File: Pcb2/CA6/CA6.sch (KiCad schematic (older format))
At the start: 119 parts, among them J1 MICRO_USB, J2 BAT_CON, J3 MODULE_0, J4 MODULE_2, J5 MODULE_1, J6 AUX, J7 AUX, J8 MODULE_3, P1 JTAG, P2 RFD22301 Breakout, Q1 BSS138P, Q10 BSS138P, Q11 BSS138P, Q12 BSS138P, Q13 BSS138P, Q14 BSS138P, Q15 BSS138P, Q16 BSS138P, Q2 BSS138P, Q3 BSS138P, Q4 BSS138P, Q5 BSS138P, Q6 BSS138P, Q7 BSS138P, Q8 BSS138P, Q9 BSS138P, SW1 ERASE, SW2 USB/BATTERY, SW3 RESET, U12 VREG_33, U14 EEPROM, U15 L_PIPE, U16 ATSAM3X8EA-AU_LQFP-144, U17 RFD22301, X1 HOLE, X10 DP, X2 HOLE, X3 HOLE, X4 DP, X6 DP, X7 CRYSTAL_4, X8 32khz, X9 DP

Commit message: Clear out old traces and make it a 2 layer board
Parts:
- removed X10, X4, X6, X9: DP, CA6:DUMMY_PIN_NEPAD_1MM, symbol DUMMY_PIN
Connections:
- no-connect marks 9 -> 14
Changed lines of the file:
@@
 AUX43
-$Comp
-L DUMMY_PIN X4
-U 1 1 5424AE5A
-P 13500 8350
-F 0 "X4" H 13950 8350 60  0000 C CNN
-F 1 "DP" H 13750 8350 60  0001 C CNN
-F 2 "CA6:DUMMY_PIN_NEPAD_1MM" H 13500 8350 60  0001 C CNN
-F 3 "~" H 13500 8350 60  0000 C CNN
-	1    13500 8350
-	1    0    0    -1
-$EndComp
-$Comp
-L DUMMY_PIN X10
-U 1 1 5424AF6F
-P 13500 8450
-F 0 "X10" H 13950 8450 60  0000 C CNN
-F 1 "DP" H 13750 8450 60  0001 C CNN
-F 2 "CA6:DUMMY_PIN_NEPAD_1MM" H 13500 8450 60  0001 C CNN
-F 3 "~" H 13500 8450 60  0000 C CNN
-	1    13500 8450
-	1    0    0    -1
-$EndComp
-$Comp
-L DUMMY_PIN X6
-U 1 1 5424AF75
-P 8400 9250
-F 0 "X6" H 8850 9250 60  0000 C CNN
-F 1 "DP" H 8650 9250 60  0001 C CNN
-F 2 "CA6:DUMMY_PIN_NEPAD_1MM" H 8400 9250 60  0001 C CNN
-F 3 "~" H 8400 9250 60  0000 C CNN
-	1    8400 9250
-	-1   0    0    1
-$EndComp
-$Comp
-L DUMMY_PIN X9
-U 1 1 5424AF81
-P 13500 6550
-F 0 "X9" H 13950 6550 60  0000 C CNN
-F 1 "DP" H 13750 6550 60  0001 C CNN
-F 2 "CA6:DUMMY_PIN_NEPAD_1MM" H 13500 6550 60  0001 C CNN
-F 3 "~" H 13500 6550 60  0000 C CNN
-	1    13500 6550
-	1    0    0    -1
-$EndComp
 $Comp
 L R R30
@@
 Connection ~ 2250 13300
 Connection ~ 1950 13600
+NoConn ~ 13500 6550
+NoConn ~ 13500 8350
+NoConn ~ 13500 8450
+NoConn ~ 8400 9250
+NoConn ~ 21400 4200
 $EndSCHEMATC

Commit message: Remove link port, only support 3.3V on aux, make board bigger, make board 2 layers, add camera port leds
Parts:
- removed C16, C35: 10uf, CA6:c_1206, symbol C
- removed D3: SCH_D, CA6:SM1206-D-A, symbol DIODESCH
- removed LP1: LINK_RJ10, CA6:RJ10_A-2004-3-4-LP-N-R, symbol JACK_RJ10
- removed R23, R24: 10k, CA6:SM0603_Resistor, symbol R
- added D10, D2, D4, D5, D6, D7, D8, D9: LED, LEDs:LED_0805, symbol LED
- added R1, R2, R3, R4, R5, R6, R7, R8: 680R, CA6:SM0603_Resistor, symbol R
- added U1, U2, U3, U4, U5, U6, U7, U8: L_PIPE, CA6:SLP3-150-100-R, symbol LED_LIGHT_PIPE
- added X4: HOLE, CA6:HOLE_3.0mm, symbol HOLE
- LOGO2: footprint CA6:CA_Logo_Mirror_15mm -> CA6:CA_Logo_15mm
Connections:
- net 3V3: now also J6.48 (PIN48), J7.48 (PIN48)
- net 5V: no longer J6.48 (PIN48), J7.48 (PIN48)
- net CAM0S: now also R1.1
- net CAM1S: now also R2.1
- net CAM2S: now also R3.1
- net CAM3S: now also R4.1
- net CAM4S: now also R5.1
- net CAM5S: now also R6.1
- net CAM6S: now also R7.1
- net CAM7S: now also R8.1
- net GND: now also D10.1 (K), D2.1 (K), D4.1 (K), D5.1 (K), D6.1 (K), D7.1 (K), D8.1 (K), D9.1 (K)
- new net: D2.2 (A), R1.2
- new net: D4.2 (A), R2.2
- new net: D5.2 (A), R3.2
- new net: D6.2 (A), R4.2
- new net: D7.2 (A), R5.2
- new net: D8.2 (A), R6.2
- new net: D9.2 (A), R7.2
- new net: D10.2 (A), R8.2
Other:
- note removed: "Link Port"

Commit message: Lots more small changes to the pcb
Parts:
- removed BT1: 4xAA_BATTERY_HOLDER, CA6:BATTERY_4AA_12BH348-GR, symbol BATTERY
- removed C26: 10uf, CA6:c_1206, symbol C
- removed C27: 0.1uf, CA6:c_0603, symbol C
- removed FTDI_2: FTDI_BLE, CA6:SIL-6, symbol FTDI
- removed U17: RFD22301, CA6:RFD22301, symbol RFD22301
- P2: footprint CA6:JTAG_20021121-00010C4LF -> Socket_Strips:Socket_Strip_Straight_2x05_Pitch2.54mm
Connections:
- net 3V3: now also C23.1, C34.1, P2.2 (PIN2); no longer C23.2, C34.2, P2.8 (PIN8)
- net GND: now also C23.2, C34.2, P2.1 (PIN1); no longer C23.1, C34.1, P2.10 (PIN10), P2.9 (PIN9)
- net at U16.13 (PD0): no longer R22.1
- net at U16.14 (PD1): no longer R30.1
- net BLE_CTS: no longer names the net of P2.4 (PIN4)
- net BLE_CTS: now also R30.1; no longer U16.8 (PA15)
- net BLE_GPIO4 renamed CC_TX
- net CC_TX: now also U16.6 (PA13)
- net BLE_GPIO5: no longer names the net of P2.6 (PIN6)
- net BLE_GPIO5: now also R22.1
- net BLE_GPIO6 renamed CC_RTS
- net CC_RTS: now also U16.7 (PA14)
- net BLE_RTS renamed CC_RX
- net CC_RX: now also U16.5 (PA12); no longer U16.7 (PA14)
- removed net BLE_RX: P2.2 (PIN2), U16.5 (PA12)
- removed net BLE_TX: P2.1 (PIN1), U16.6 (PA13)
- net LP_FOCUS: no longer names the net of U16.59 (PC2)
- net LP_SHUTTER: no longer names the net of U16.60 (PC3)
- new net CC_CTS: P2.9 (PIN9), U16.8 (PA15)
- new net CC_PROG: P2.10 (PIN10)
- new net CC_RESET: P2.8 (PIN8)
- no-connect marks 14 -> 8
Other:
- note added: "Connectivity Card"
- note removed: "Bluetooth"
- moved on the sheet: C23, C30, C31, C32, C33, C34, C37, D1, J3, J4, J5, J6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

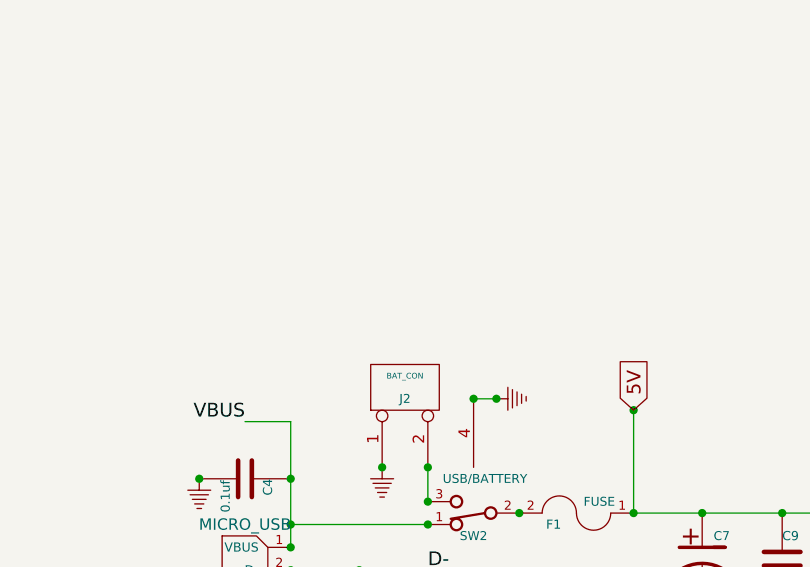
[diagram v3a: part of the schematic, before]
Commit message: Clean up layout and add ground plane
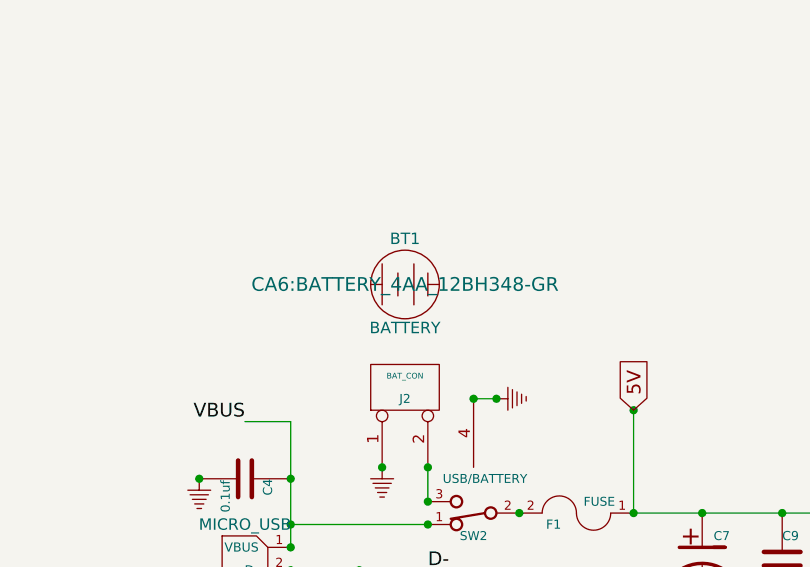
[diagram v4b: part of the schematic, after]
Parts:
- added BT1: BATTERY, CA6:BATTERY_4AA_12BH348-GR, symbol BATTERY
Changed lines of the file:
@@
 	18200 12700 18150 12700
 Connection ~ 18150 12700
+$Comp
+L BATTERY BT1
+U 1 1 58D3FF70
+P 7400 12800
+F 0 "BT1" H 7400 13000 50  0000 C CNN
+F 1 "BATTERY" H 7400 12610 50  0000 C CNN
+F 2 "CA6:BATTERY_4AA_12BH348-GR" H 7400 12800 60  0000 C CNN
+F 3 "" H 7400 12800 60  0000 C CNN
+	1    7400 12800
+	1    0    0    -1
+$EndComp
 $EndSCHEMATC

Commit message: Routing pcb
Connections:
- net 3V3: no longer J6.48 (PIN48), J7.48 (PIN48)
- net AUX02: now also U16.141 (PB22); no longer U16.136 (PC25)
- net AUX03: now also U16.140 (PB14); no longer U16.135 (PC24)
- net AUX04: now also U16.138 (PC27); no longer U16.134 (PC23)
- net AUX05: now also U16.137 (PC26); no longer U16.133 (PC22)
- net AUX06: now also U16.136 (PC25); no longer U16.132 (PC21)
- net AUX07: now also U16.135 (PC24); no longer U16.131 (PC20)
- net AUX08: now also U16.134 (PC23); no longer U16.128 (PB10)
- net AUX09: now also U16.133 (PC22); no longer U16.127 (PB9)
- net AUX10: now also U16.132 (PC21); no longer U16.123 (PB8)
- net AUX11: now also U16.131 (PC20); no longer U16.122 (PB7)
- net AUX12: now also U16.128 (PB10); no longer U16.121 (PB6)
- net AUX13: now also U16.127 (PB9); no longer U16.120 (PB5)
- net AUX14: now also U16.123 (PB8); no longer U16.119 (PB4)
- net AUX15: now also U16.122 (PB7); no longer U16.118 (PB3)
- net AUX16: now also U16.121 (PB6); no longer U16.117 (PC10)
- net AUX17: now also U16.120 (PB5); no longer U16.116 (PC4)
- net AUX18: now also U16.119 (PB4); no longer U16.115 (PB2)
- net AUX19: now also U16.118 (PB3); no longer U16.114 (PB1)
- net AUX20: now also U16.117 (PC10); no longer U16.113 (PB0)
- net AUX21: now also U16.116 (PC4); no longer U16.112 (PA29)
- net AUX22: now also U16.115 (PB2); no longer U16.103 (PC30)
- net AUX23: now also U16.114 (PB1); no longer U16.102 (PC29)
- net AUX24: now also U16.113 (PB0); no longer U16.101 (PC19)
- net AUX25: now also U16.112 (PA29); no longer U16.100 (PC18)
- net AUX26: now also U16.103 (PC30); no longer U16.99 (PC17)
- net AUX27: now also U16.102 (PC29); no longer U16.98 (PC16)
- net AUX28: now also U16.101 (PC19); no longer U16.97 (PC15)
- net AUX29: now also U16.100 (PC18); no longer U16.96 (PC14)
- net AUX30: now also U16.99 (PC17); no longer U16.95 (PC13)
- net AUX31: now also U16.98 (PC16); no longer U16.94 (PC12)
- net AUX32: now also U16.97 (PC15); no longer U16.93 (PC11)
- net AUX33: now also U16.96 (PC14); no longer U16.92 (PB21)
- net AUX34: now also U16.95 (PC13); no longer U16.91 (PB20)
- net AUX35: now also U16.94 (PC12); no longer U16.90 (PB19)
- net AUX36: now also U16.93 (PC11); no longer U16.89 (PB18)
- net AUX37: now also U16.92 (PB21); no longer U16.77 (PB16)
- net AUX38: now also U16.91 (PB20); no longer U16.76 (PB15)
- net AUX39: now also U16.90 (PB19); no longer U16.72 (PA20)
- net AUX40: now also U16.89 (PB18); no longer U16.71 (PA19)
- net AUX41: now also U16.77 (PB16); no longer U16.68 (PB27)
- net AUX42: now also U16.76 (PB15); no longer U16.67 (PC9)
- net AUX43: now also U16.72 (PA20); no longer U16.66 (PC8)
- net AUX_RX: now also J6.2 (PIN2), J7.2 (PIN2); no longer J6.46 (PIN46), J7.46 (PIN46)
- net AUX_TX: now also J6.1 (PIN1), J7.1 (PIN1); no longer J6.45 (PIN45), J7.45 (PIN45)
- net CAM0F: now also U16.142 (PB23); no longer U16.140 (PB14)
- net CAM0S: now also U16.143 (PB24); no longer U16.141 (PB22)
- net CAM1F: now also U16.144 (PB25); no longer U16.142 (PB23)
- net CAM1S: now also U16.1 (PB26); no longer U16.143 (PB24)
- net CAM2F: now also U16.13 (PD0); no longer U16.144 (PB25)
- net CAM2S: now also U16.14 (PD1); no longer U16.1 (PB26)
- net CC_PROG: now also U16.59 (PC2)
- net CC_RESET: now also U16.55 (PC1)
- net GND: no longer J6.47 (PIN47), J7.47 (PIN47)
- net MOD3_ID: now also U16.60 (PC3); no longer U16.55 (PC1)
- removed net AUX00: J6.1 (PIN1), J7.1 (PIN1), U16.138 (PC27)
- removed net AUX01: J6.2 (PIN2), J7.2 (PIN2), U16.137 (PC26)
- new net AUX44: J6.45 (PIN45), J7.45 (PIN45), U16.71 (PA19)
- new net AUX45: J6.46 (PIN46), J7.46 (PIN46), U16.68 (PB27)
- new net AUX46: J6.47 (PIN47), J7.47 (PIN47), U16.67 (PC9)
- new net AUX47: J6.48 (PIN48), J7.48 (PIN48), U16.66 (PC8)
- no-connect marks 8 -> 7
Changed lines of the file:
@@
 Text Notes 1900 3350 0    118  ~ 24
 JTAG
-Text Notes 18500 14200 0    118  ~ 24
+Text Notes 18850 13900 0    118  ~ 24
 Connectivity Card
 Text Notes 9000 15350 0    118  ~ 24
@@
 	0    -1   -1   0
 $EndComp
-Text Label 13650 900  0    60   ~ 0
-AUX01
+Text Label 13650 3100 0    60   ~ 0
+AUX45
 Text Label 3650 2350 0    60   ~ 0
 JTAG_TMS
@@
 Text Label 6900 2550 2    60   ~ 0
 EEPROM_ID
-Text Label 12150 900  2    60   ~ 0
-AUX00
+Text Label 12150 3100 2    60   ~ 0
+AUX44
 Text Label 12150 1000 2    60   ~ 0
 AUX02
@@
 Text Label 13650 1800 0    60   ~ 0
 AUX19
-Text Label 8400 9150 2    60   ~ 0
-AUX00
 Text Label 19250 6300 0    60   ~ 0
 MOD0_AN1
@@
 Text Label 9200 5750 1    60   ~ 0
 MOD3_MISO
-Text Label 8400 7350 2    60   ~ 0
+Text Label 8400 8050 2    60   ~ 0
 AUX13
-Text Label 8400 7250 2    60   ~ 0
+Text Label 8400 7650 2    60   ~ 0
 AUX14
-Text Label 8400 7150 2    60   ~ 0
+Text Label 8400 7550 2    60   ~ 0
 AUX15
-Text Label 8400 7050 2    60   ~ 0
+Text Label 8400 7450 2    60   ~ 0
 AUX16
-Text Label 8400 6950 2    60   ~ 0
+Text Label 8400 7350 2    60   ~ 0
 AUX17
-Text Label 8400 6850 2    60   ~ 0
+Text Label 8400 7250 2    60   ~ 0
 AUX18
-Text Label 8400 6750 2    60   ~ 0
+Text Label 8400 7150 2    60   ~ 0
 AUX19
-Text Label 8400 6650 2    60   ~ 0
+Text Label 8400 7050 2    60   ~ 0
 AUX20
-Text Label 8400 6550 2    60   ~ 0
+Text Label 8400 6950 2    60   ~ 0
 AUX21
-Text Label 9700 5750 1    60   ~ 0
+Text Label 8400 6850 2    60   ~ 0
 AUX22
-Text Label 9800 5750 1    60   ~ 0
+Text Label 8400 6750 2    60   ~ 0
 AUX23
-Text Label 9900 5750 1    60   ~ 0
+Text Label 8400 6650 2    60   ~ 0
 AUX24
-Text Label 10000 5750 1    60   ~ 0
+Text Label 8400 6550 2    60   ~ 0
 AUX25
-Text Label 10100 5750 1    60   ~ 0
+Text Label 9700 5750 1    60   ~ 0
 AUX26
-Text Label 10200 5750 1    60   ~ 0
+Text Label 9800 5750 1    60   ~ 0
 AUX27
 Text Label 11300 5750 1    60   ~ 0
@@
 Text Label 9300 5750 1    60   ~ 0
 EEPROM_ID
-Text Label 8400 9350 2    60   ~ 0
+Text Label 8400 9550 2    60   ~ 0
 CAM0F
-Text Label 8400 9450 2    60   ~ 0
+Text Label 8400 9650 2    60   ~ 0
 CAM0S
-Text Label 8400 9550 2    60   ~ 0
+Text Label 8400 9750 2    60   ~ 0
 CAM1F
-Text Label 8400 9650 2    60   ~ 0
+Text Label 9200 10250 3    60   ~ 0
 CAM1S
 Text Label 8400 8250 2    60   ~ 0
 UOTGID
-Text Label 8400 9750 2    60   ~ 0
+Text Label 10400 10250 3    60   ~ 0
 CAM2F
-Text Label 9200 10250 3    60   ~ 0
+Text Label 10500 10250 3    60   ~ 0
 CAM2S
 Text Label 10600 10250 3    60   ~ 0
@@
 Text Label 12200 5750 1    60   ~ 0
 MOD3_AN1
-Text Label 10300 5750 1    60   ~ 0
+Text Label 9900 5750 1    60   ~ 0
 AUX28
-Text Label 10400 5750 1    60   ~ 0
+Text Label 10000 5750 1    60   ~ 0
 AUX29
-Text Label 10800 5750 1    60   ~ 0
+Text Label 10400 5750 1    60   ~ 0
 AUX33
-Text Label 10900 5750 1    60   ~ 0
+Text Label 10500 5750 1    60   ~ 0
 AUX34
 $Comp
@@
 	1    0    0    -1
 $EndComp
-Text Label 11100 5750 1    60   ~ 0
+Text Label 10700 5750 1    60   ~ 0
 AUX36
-Text Label 12400 5750 1    60   ~ 0
+Text Label 10900 5750 1    60   ~ 0
 AUX38
 Text Label 11800 10250 3    60   ~ 0
 AUX_RX
-Text Label 11000 5750 1    60   ~ 0
+Text Label 10600 5750 1    60   ~ 0
 AUX35
 $Comp
@@
 	1    0    0    -1
 $EndComp
-Text Label 12150 3100 2    60   ~ 0
+Text Label 12150 900  2    60   ~ 0
 AUX_TX
 $Comp
@@
 Text Label 21100 7750 2    60   ~ 0
 MOD3_CS
-Text Label 12300 5750 1    60   ~ 0
+Text Label 10800 5750 1    60   ~ 0
 AUX37
-Text Label 8400 9050 2    60   ~ 0
-AUX01
-Text Label 8400 8950 2    60   ~ 0
+Text Label 8400 9450 2    60   ~ 0
 AUX02
-Text Label 8400 8850 2    60   ~ 0
+Text Label 8400 9350 2    60   ~ 0
 AUX03
-Text Label 8400 8750 2    60   ~ 0
+Text Label 8400 9150 2    60   ~ 0
 AUX04
-Text Label 8400 8650 2    60   ~ 0
+Text Label 8400 9050 2    60   ~ 0
 AUX05
-Text Label 8400 8550 2    60   ~ 0
+Text Label 8400 8950 2    60   ~ 0
 AUX06
-Text Label 8400 8450 2    60   ~ 0
+Text Label 8400 8850 2    60   ~ 0
 AUX07
-Text Label 8400 8150 2    60   ~ 0
+Text Label 8400 8750 2    60   ~ 0
 AUX08
-Text Label 8400 8050 2    60   ~ 0
+Text Label 8400 8650 2    60   ~ 0
 AUX09
-Text Label 8400 7650 2    60   ~ 0
+Text Label 8400 8550 2    60   ~ 0
 AUX10
-Text Label 8400 7450 2    60   ~ 0
+Text Label 8400 8150 2    60   ~ 0
 AUX12
-Text Label 8400 7550 2    60   ~ 0
+Text Label 8400 8450 2    60   ~ 0
 AUX11
 Text Label 13500 7150 0    60   ~ 0
 MOD2_ID
-Text Label 10700 5750 1    60   ~ 0
+Text Label 10300 5750 1    60   ~ 0
 AUX32
-Text Label 10600 5750 1    60   ~ 0
+Text Label 10200 5750 1    60   ~ 0
 AUX31
-Text Label 10500 5750 1    60   ~ 0
+Text Label 10100 5750 1    60   ~ 0
 AUX30
 $Comp
@@
 	1    0    0    -1
 $EndComp
-Text Label 13500 7950 0    60   ~ 0
+Text Label 13500 7450 0    60   ~ 0
 MOD3_ID
 $Comp
@@
 	1    0    0    -1
 $EndComp
-Text Label 13650 3100 0    60   ~ 0
+Text Label 13650 900  0    60   ~ 0
 AUX_RX
-Text Label 16450 900  0    60   ~ 0
-AUX01
-Text Label 14950 900  2    60   ~ 0
-AUX00
 Text Label 14950 1000 2    60   ~ 0
 AUX02
@@
 Text Label 16450 3000 0    60   ~ 0
 AUX43
-Text Label 14950 3100 2    60   ~ 0
+Text Label 14950 900  2    60   ~ 0
 AUX_TX
 $Comp
@@
 	1    0    0    -1
 $EndComp
-Text Label 16450 3100 0    60   ~ 0
+Text Label 16450 900  0    60   ~ 0
 AUX_RX
 $Comp
@@
 	1    0    0    -1
 $EndComp
-Text Label 13500 6650 0    60   ~ 0
+Text Label 12300 5750 1    60   ~ 0
 AUX41
-Text Label 13500 6250 0    60   ~ 0
+Text Label 11000 5750 1    60   ~ 0
 AUX39
-Text Label 13500 6350 0    60   ~ 0
+Text Label 11100 5750 1    60   ~ 0
 AUX40
-Text Label 13500 6750 0    60   ~ 0
+Text Label 12400 5750 1    60   ~ 0
 AUX42
-Text Label 13500 6850 0    60   ~ 0
+Text Label 13500 6250 0    60   ~ 0
 AUX43
 $Comp
@@
 Connection ~ 13650 3700
 Connection ~ 12150 3300
-Connection ~ 12150 900
-Connection ~ 12150 1000
-Connection ~ 12150 1100
-Connection ~ 12150 1200
-Connection ~ 12150 1300
-Connection ~ 12150 1400
-Connection ~ 12150 1500
-Connection ~ 12150 1600
-Connection ~ 12150 1700
-Connection ~ 12150 1800
-Connection ~ 12150 1900
-Connection ~ 12150 2000
-Connection ~ 12150 2100
-Connection ~ 12150 2200
-Connection ~ 12150 2300
-Connection ~ 12150 2400
-Connection ~ 12150 2500
-Connection ~ 12150 2600
-Connection ~ 12150 2700
-Connection ~ 12150 2800
-Connection ~ 12150 2900
-Connection ~ 12150 3000
-Connection ~ 12150 3100
-Connection ~ 12150 3200
-Connection ~ 13650 3000
-Connection ~ 13650 2900
-Connection ~ 13650 2800
-Connection ~ 13650 2700
-Connection ~ 13650 2600
-Connection ~ 13650 2500
-Connection ~ 13650 2400
-Connection ~ 13650 2300
-Connection ~ 13650 2200
-Connection ~ 13650 2100
-Connection ~ 13650 2000
-Connection ~ 13650 1900
-Connection ~ 13650 1800
-Connection ~ 13650 1700
-Connection ~ 13650 1600
-Connection ~ 13650 1500
-Connection ~ 13650 1400
-Connection ~ 13650 1300
-Connection ~ 13650 1200
-Connection ~ 13650 1100
-Connection ~ 13650 1000
-Connection ~ 13650 900
 Connection ~ 8400 13350
 Connection ~ 8400 13800
@@
 Connection ~ 19900 7550
 Wire Wire Line
-	12150 3200 12150 3300
-Wire Wire Line
 	7900 13800 7900 13800
 Connection ~ 7900 13800
@@
 Connection ~ 16450 3300
 Connection ~ 14950 3300
-Connection ~ 14950 900
-Connection ~ 14950 1000
-Connection ~ 14950 1100
-Connection ~ 14950 1200
-Connection ~ 14950 1300
-Connection ~ 14950 1400
-Connection ~ 14950 1500
-Connection ~ 14950 1600
-Connection ~ 14950 1700
-Connection ~ 14950 1800
-Connection ~ 14950 1900
-Connection ~ 14950 2000
-Connection ~ 14950 2100
-Connection ~ 14950 2200
-Connection ~ 14950 2300
-Connection ~ 14950 2400
-Connection ~ 14950 2500
-Connection ~ 14950 2600
-Connection ~ 14950 2700
-Connection ~ 14950 2800
-Connection ~ 14950 2900
-Connection ~ 14950 3000
-Connection ~ 14950 3100
-Connection ~ 14950 3200
-Connection ~ 16450 3200
-Connection ~ 16450 3000
-Connection ~ 16450 2900
-Connection ~ 16450 2800
-Connection ~ 16450 2700
-Connection ~ 16450 2600
-Connection ~ 16450 2500
-Connection ~ 16450 2400
-Connection ~ 16450 2300
-Connection ~ 16450 2200
-Connection ~ 16450 2100
-Connection ~ 16450 2000
-Connection ~ 16450 1900
-Connection ~ 16450 1800
-Connection ~ 16450 1700
-Connection ~ 16450 1600
-Connection ~ 16450 1500
-Connection ~ 16450 1400
-Connection ~ 16450 1300
-Connection ~ 16450 1200
-Connection ~ 16450 1100
-Connection ~ 16450 1000
-Connection ~ 16450 900
 Connection ~ 17000 3300
-Wire Wire Line
-	14950 3200 14950 3300
 Connection ~ 9600 14500
 Wire Wire Line
@@
 NoConn ~ 13500 8450
 NoConn ~ 8400 9250
-NoConn ~ 13800 850
 $Comp
 L LED_LIGHT_PIPE U1
@@
 	1    0    0    -1
 $EndComp
-Wire Wire Line
-	13650 3300 13650 3200
-Wire Wire Line
-	16450 3200 16450 3300
-Connection ~ 13650 3200
 $Comp
 L HOLE X4
@@
 F 0 "BT1" H 7400 13000 50  0000 C CNN
 F 1 "BATTERY" H 7400 12610 50  0000 C CNN
-F 2 "CA6:BATTERY_4AA_12BH348-GR" H 7400 12800 60  0000 C CNN
+F 2 "CA6:BATTERY_4AA_12BH348-GR" H 7400 12800 60  0001 C CNN
 F 3 "" H 7400 12800 60  0000 C CNN
 	1    7400 12800
 	1    0    0    -1
 $EndComp
+Text Label 13500 7950 0    60   ~ 0
+CC_RESET
+Text Label 13500 7550 0    60   ~ 0
+CC_PROG
+Text Label 12150 3200 2    60   ~ 0
+AUX46
+Text Label 13650 3200 0    60   ~ 0
+AUX47
+Text Label 13500 6350 0    60   ~ 0
+AUX44
+Text Label 13500 6650 0    60   ~ 0
+AUX45
+Text Label 13500 6750 0    60   ~ 0
+AUX46
+Text Label 13500 6850 0    60   ~ 0
+AUX47
+Text Label 14950 3100 2    60   ~ 0
+AUX44
+Text Label 14950 3200 2    60   ~ 0
+AUX46
+Text Label 16450 3100 0    60   ~ 0
+AUX45
+Text Label 16450 3200 0    60   ~ 0
+AUX47
 $EndSCHEMATC

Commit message: More updates on pcb layout
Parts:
- P2: footprint Socket_Strips:Socket_Strip_Straight_2x05_Pitch2.54mm -> Socket_Strips:Socket_Strip_Straight_1x10_Pitch2.54mm
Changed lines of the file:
@@
 F 0 "P2" H 18950 13350 50  0000 C CNN
 F 1 "RFD22301 Breakout" H 18950 12700 39  0000 C CNN
-F 2 "Socket_Strips:Socket_Strip_Straight_2x05_Pitch2.54mm" H 18950 13050 50  0001 C CNN
+F 2 "Socket_Strips:Socket_Strip_Straight_1x10_Pitch2.54mm" H 18950 13050 50  0001 C CNN
 F 3 "DOCUMENTATION" H 18950 13050 50  0001 C CNN
 	1    18950 13050
